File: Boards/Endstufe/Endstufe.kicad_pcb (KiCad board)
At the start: 2 copper layers, 153 x 111 mm, 64 parts, among them J1 HV In, J2 Relais, J3 NF_In, J4 Trafo, K1 G6E, P4 6V3_AC, P5 Trafo_GK, P6 6V3_DC, P7 VSup1, P8 Bias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

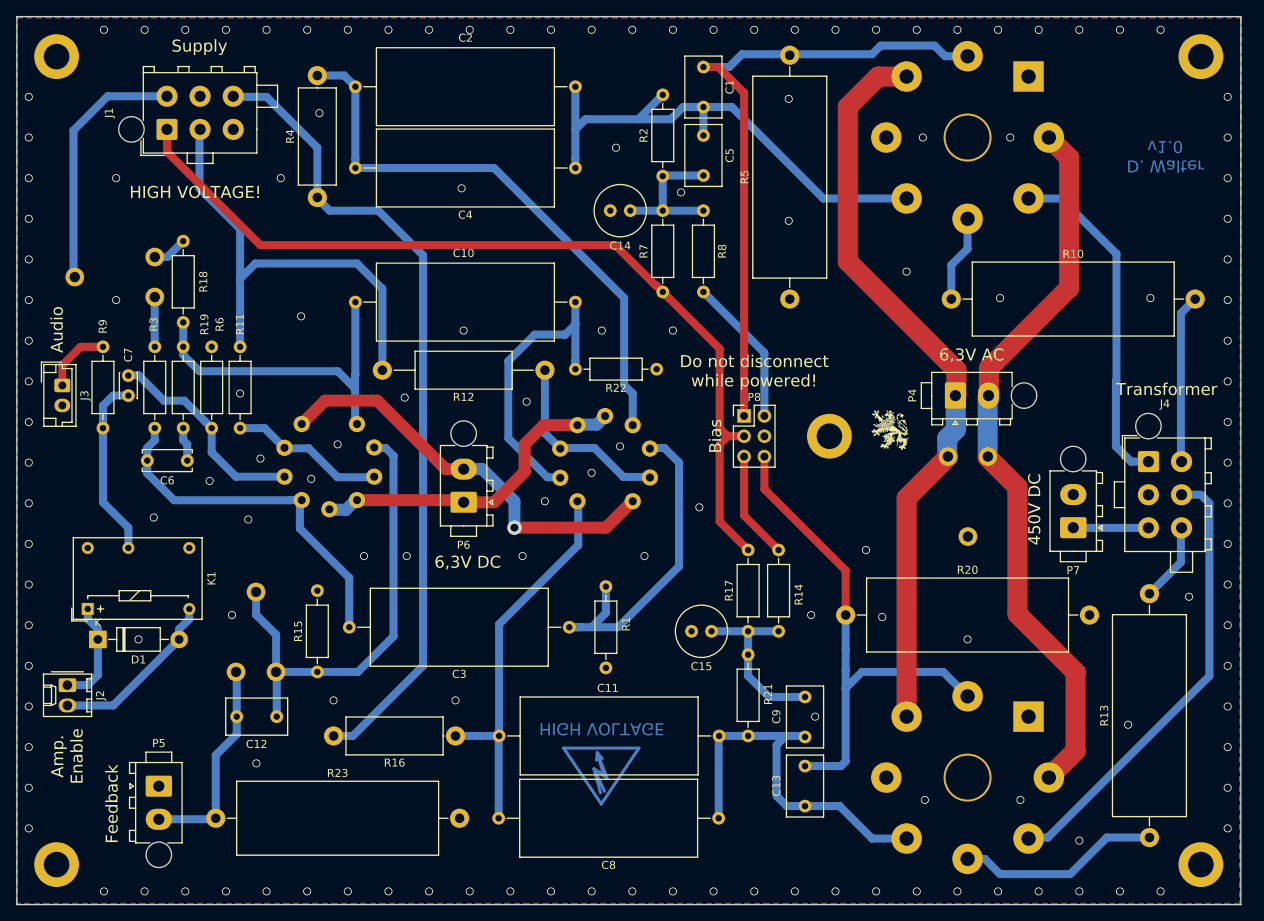
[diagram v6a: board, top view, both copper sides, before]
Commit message: Added Mounting holes, Moved -60V Divider to HV Board, eliminated +450V Connector and Feedback Connector on Amp Board
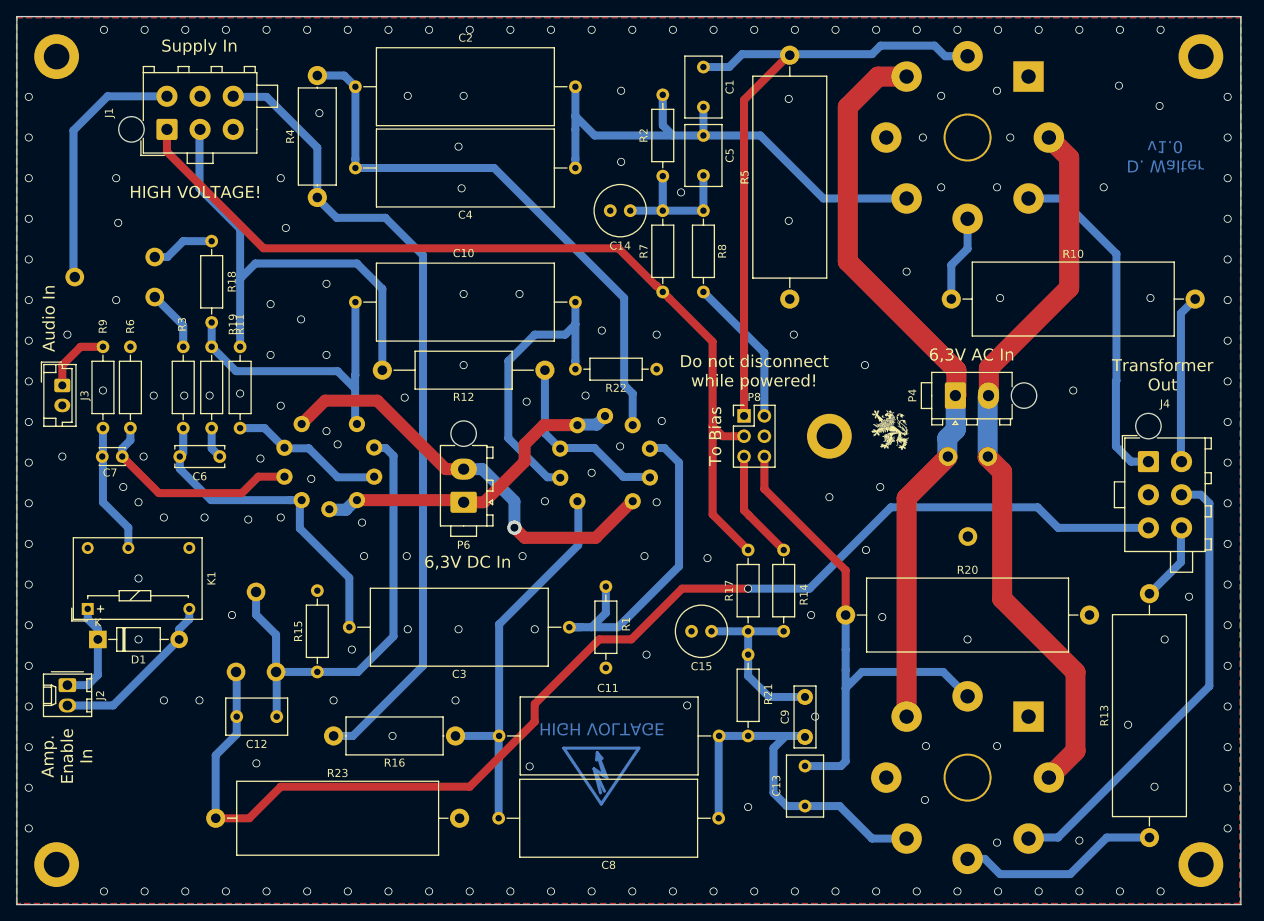
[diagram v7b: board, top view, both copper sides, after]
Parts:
- removed P5: Trafo_GK, Connector_TE-Connectivity:TE_MATE-N-LOK_1-770866-x_1x02_P4.14mm_Vertical
- removed P7: VSup1, Connector_TE-Connectivity:TE_MATE-N-LOK_1-770866-x_1x02_P4.14mm_Vertical
- C9: footprint Capacitor_THT:C_Disc_D7.5mm_W4.4mm_P5.00mm -> Capacitor_THT:C_Disc_D7.5mm_W2.5mm_P5.00mm
- moved R6 10.2 mm to (73.2, 92.5)
- moved C7 8.29 mm to (69.6, 106.2), turned to 0 degrees
- moved C6 4.10 mm to (84.3, 106.2)
- moved R18 3.56 mm to (83.3, 89.4)
- moved R19 3.56 mm to (83.3, 92.5)
- moved R3 3.56 mm to (79.8, 92.5)
- moved R14 0.63 mm to (154.8, 128.0)
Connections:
- J4 pad 3: +450V -> Net-(C12-Pad2)
- K1 pad 12: Net-(K1-Pad12) -> (no net)
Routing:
- net Net-(C12-Pad2): track 26.6 -> 154.5 mm, vias 0 -> 1
- net +450V: track 9.41 -> 0.00 mm
- net Net-(C7-Pad1): track 22.8 -> 16.3 mm
- net Net-(C3-Pad2): track 45.1 -> 40.5 mm
- net Net-(C10-Pad2): track 42.6 -> 38.5 mm
- net Net-(R18-Pad2): track 4.38 -> 7.93 mm
- net -60V: track 111.6 -> 113.2 mm
- net Net-(R3-Pad1): track 6.22 -> 7.70 mm
- net Net-(P6-Pad2): track 52.5 -> 53.5 mm
- net Net-(P6-Pad1): track 41.5 -> 40.8 mm
- net Net-(J4-Pad5): track 56.5 -> 57.3 mm
- net Bias_1: track 81.6 -> 82.3 mm
- net Net-(C15-Pad1): track 22.2 -> 22.8 mm
- net Net-(C14-Pad1): track 18.6 -> 18.0 mm
- net GND: vias 142 -> 198
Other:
- board text added: "6,3V AC In"
- board text added: "6,3V DC In"
- board text added: "Amp. Enable In"
- board text added: "Audio In"
- board text added: "KT88 Heater Adjust"
- board text added: "Supply In"
- board text added: "To Bias"
- board text added: "Transformer Out"
- board text removed: "450V DC"
- board text removed: "6,3V AC"
- board text removed: "6,3V DC"
- board text removed: "Amp. Enable"
- board text removed: "Audio"
- board text removed: "Bias"
- board text removed: "Feedback"
- board text removed: "Heater Adjust"
- board text removed: "Supply"
- board text removed: "Transformer"

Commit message: 6,3V und 12V auf einer Platine zusammengefasst
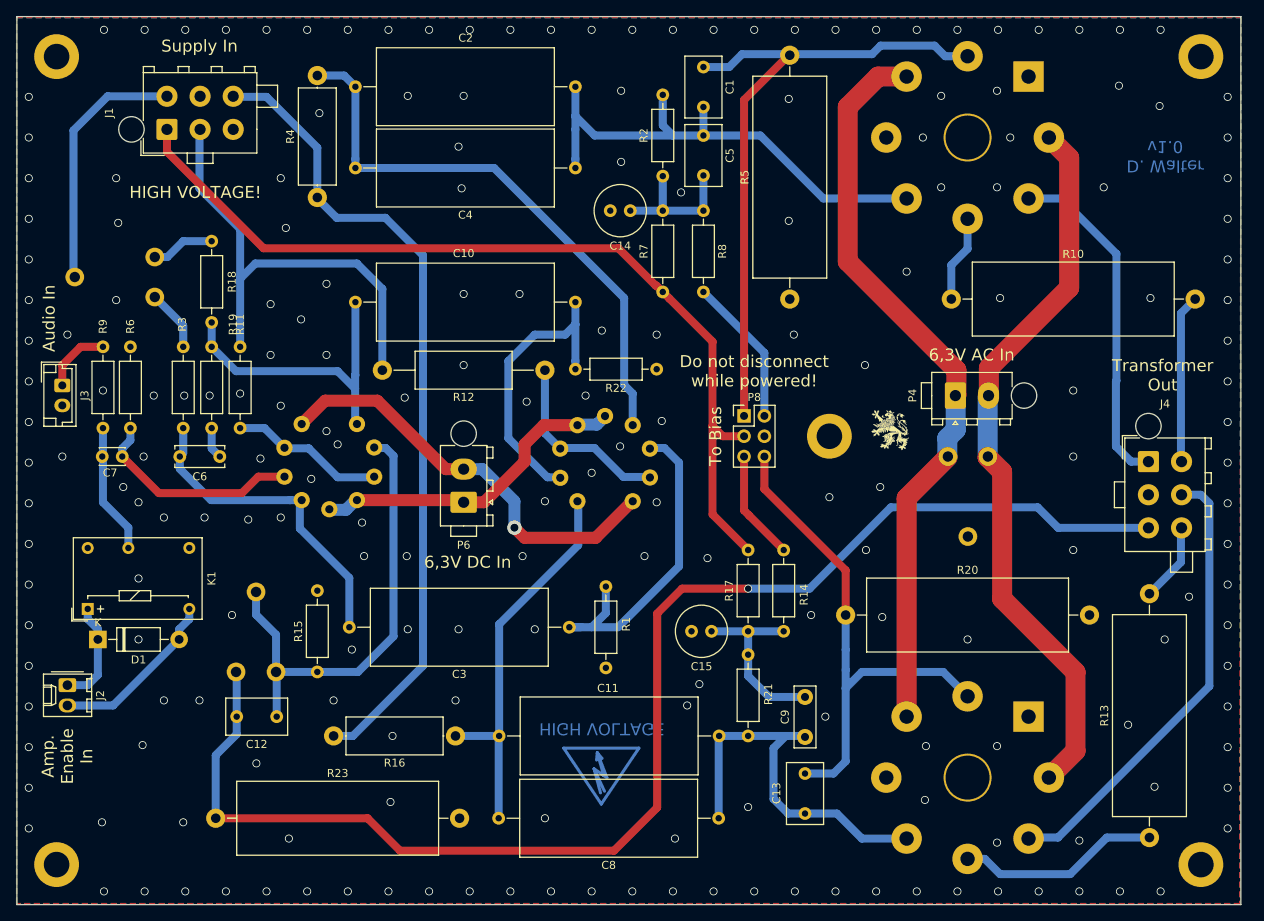
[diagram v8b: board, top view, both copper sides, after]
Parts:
- moved C13 0.94 mm to (157.5, 145.8)
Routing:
- net Net-(C12-Pad2): track 154.5 -> 170.8 mm
- net GND: vias 198 -> 206
